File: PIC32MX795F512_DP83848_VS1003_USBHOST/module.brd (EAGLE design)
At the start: 109.9 x 68.6 mm, 116 parts, among them IC1 IC_USBLC6-2, IC2 LM1117IMPX-3.3, IC3 PIC32MX795F512, IC4 DP83848, IC5 LM1117MPX-2.5, U1 USD-SOCKETUSD, U2 VS1003, X2 CRYSTALS-NOGND-CFPX-217, X3 KUSBVX, Y1 CRYSTAL-GROUNDEDSMD-5X3.2, Y3 CRYSTAL-GROUNDEDSMD-5X3.2

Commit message: PCB updates
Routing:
- net GND: track 72.8 -> 73.7 mm
- added copper zone on layer 1, net N$4
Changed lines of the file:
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@@
 <wire x1="49.492" y1="48.3488" x2="48.88" y2="48.9608" width="0.2032" layer="1"/>
 <wire x1="47.468" y1="48.9608" x2="48.88" y2="48.9608" width="0.2032" layer="1"/>
-<wire x1="43.692" y1="42.0938" x2="45.5362" y2="42.0938" width="0.2032" layer="1"/>
-<wire x1="45.5362" y1="42.0938" x2="45.72" y2="41.91" width="0.2032" layer="1"/>
 <wire x1="55.092" y1="32.6938" x2="57.3304" y2="32.6938" width="0.19811875" layer="1"/>
 <via x="26.5324" y="34.7218" extent="1-16" drill="0.6" diameter="1.4224" shape="octagon"/>
@@
 <contactref element="SV1" pad="6"/>
 <contactref element="SV1" pad="4"/>
+<wire x1="43.692" y1="40.0938" x2="46.7614" y2="40.0938" width="0.2032" layer="1"/>
 </signal>
 <signal name="3V">
@@
 <wire x1="8.6868" y1="35.7632" x2="8.6868" y2="35.7736" width="0.3048" layer="1"/>
 </signal>
+<signal name="N$4">
+<polygon width="0" layer="1" pour="cutout">
+<vertex x="42.164" y="42.4434"/>
+<vertex x="42.164" y="39.37"/>
+<vertex x="45.2628" y="39.37"/>
+<vertex x="45.2628" y="42.4434"/>
+</polygon>
+</signal>
 </signals>

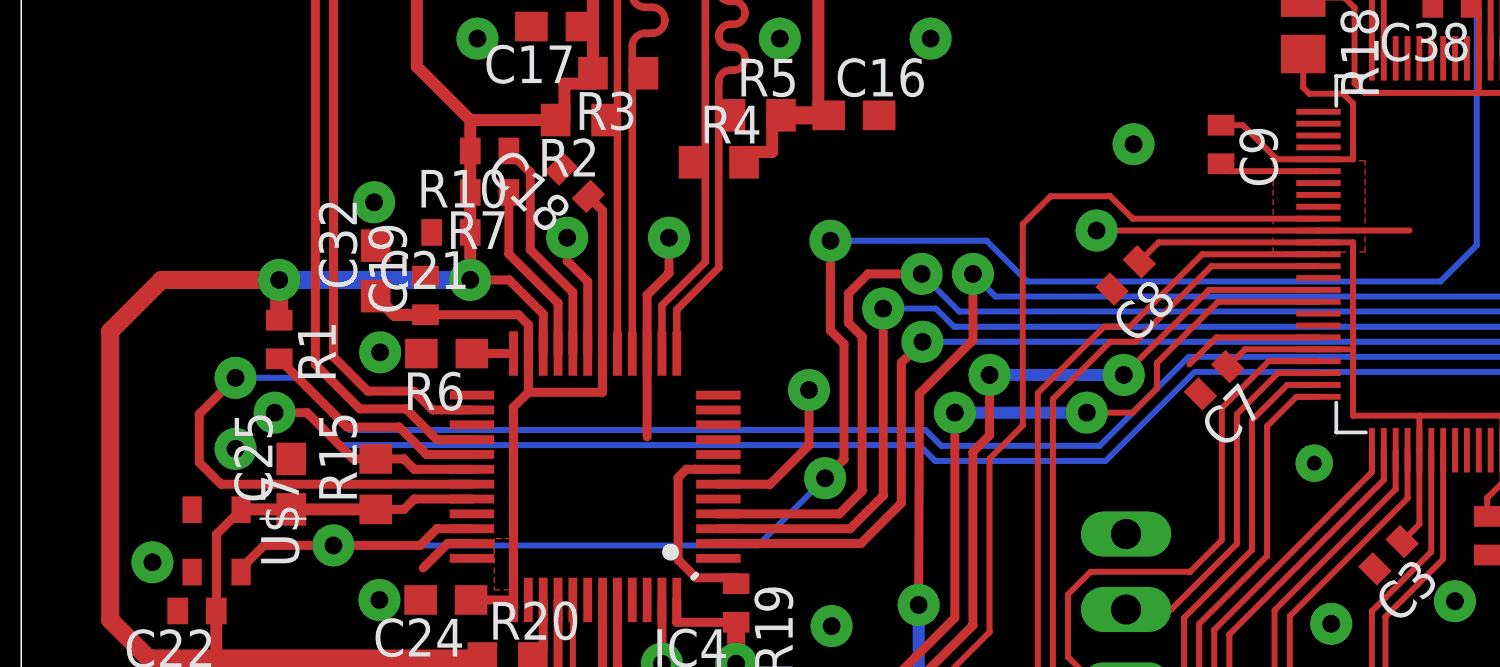
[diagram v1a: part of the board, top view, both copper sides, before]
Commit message: DP83848 RST line added
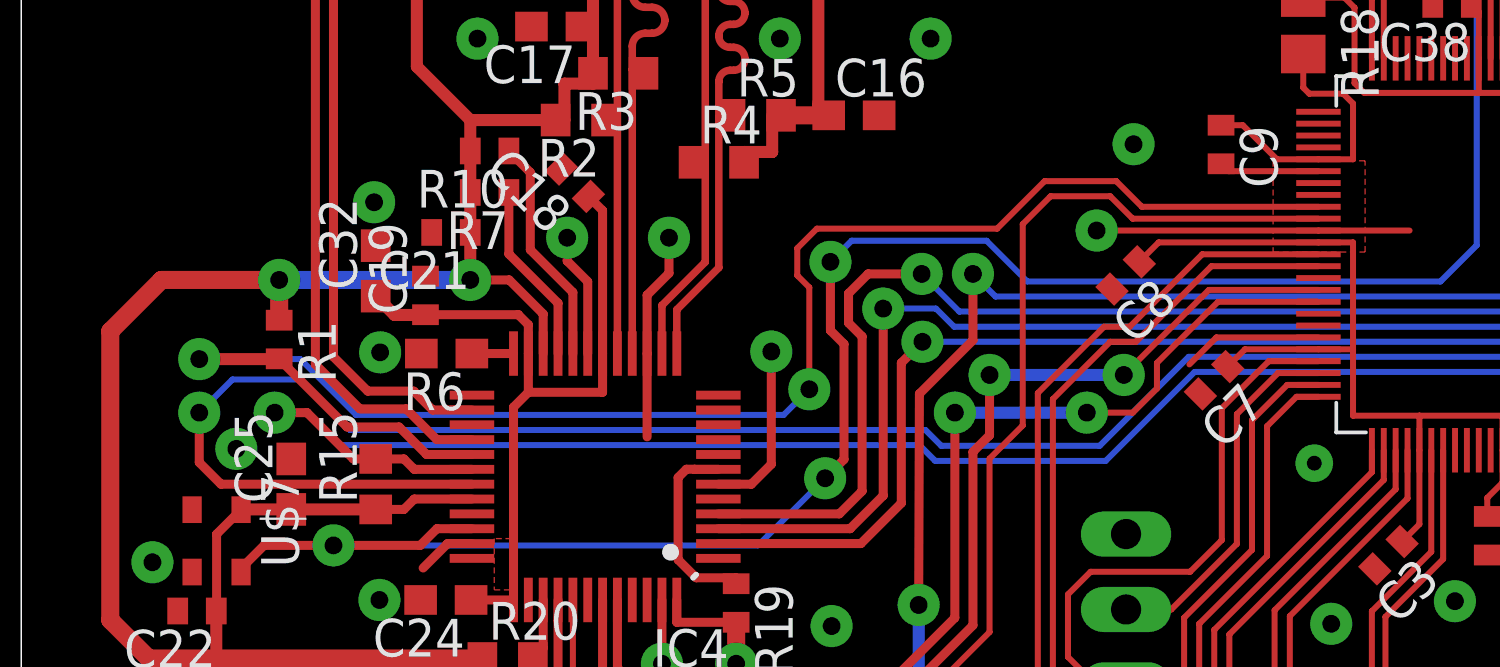
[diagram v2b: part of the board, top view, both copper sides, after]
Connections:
- removed net N$2: IC4.29, R1.2
- new net DP_RST: IC3.34, IC4.29, R1.2
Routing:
- net DP_RST: track 0.00 -> 56.0 mm, vias 0 -> 2
- net N$2: track 7.83 -> 0.00 mm
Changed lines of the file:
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@@
 <wire x1="18.387" y1="39.0678" x2="19.0794" y2="38.3754" width="0.3048" layer="1"/>
 <contactref element="U$7" pad="2"/>
-<via x="7.2176" y="32.7406" extent="1-16" drill="0.6" diameter="1.4224" shape="octagon"/>
+<via x="7.243" y="32.7406" extent="1-16" drill="0.6" diameter="1.4224" shape="octagon"/>
 <via x="4.417" y="28.9208" extent="1-16" drill="0.6" diameter="1.4224" shape="octagon"/>
 <via x="15.3644" y="46.5582" extent="1-16" drill="0.6" diameter="1.4224" shape="octagon"/>
@@
 <wire x1="47.468" y1="48.9608" x2="48.88" y2="48.9608" width="0.2032" layer="1"/>
 <wire x1="55.092" y1="32.6938" x2="57.3304" y2="32.6938" width="0.19811875" layer="1"/>
-<via x="26.5324" y="34.7218" extent="1-16" drill="0.6" diameter="1.4224" shape="octagon"/>
+<via x="25.2624" y="36.0172" extent="1-16" drill="0.6" diameter="1.4224" shape="octagon"/>
 <wire x1="21.0794" y1="35.9508" x2="21.0794" y2="33.1444" width="0.3048" layer="1"/>
 <via x="27.2944" y="26.7716" extent="1-16" drill="0.6" diameter="1.4224" shape="octagon"/>
@@
 <wire x1="43.692" y1="40.0938" x2="36.2204" y2="40.0938" width="0.2032" layer="1"/>
 <via x="54.384" y="19.431" extent="1-16" drill="0.6" diameter="1.4224" shape="octagon"/>
-<wire x1="23.4794" y1="31.5508" x2="25.2262" y2="31.5508" width="0.3048" layer="1"/>
-<wire x1="25.2262" y1="31.5508" x2="26.5324" y2="32.857" width="0.3048" layer="1"/>
-<wire x1="26.5324" y1="34.7218" x2="26.5324" y2="32.857" width="0.3048" layer="1"/>
+<wire x1="23.4794" y1="31.5508" x2="24.5912" y2="31.5508" width="0.3048" layer="1"/>
+<wire x1="24.5912" y1="31.5508" x2="25.2624" y2="32.222" width="0.3048" layer="1"/>
 <via x="59.5656" y="24.7396" extent="1-16" drill="0.6" diameter="1.4224" shape="octagon"/>
 <contactref element="SV1" pad="5"/>
@@
 <contactref element="SV1" pad="4"/>
 <wire x1="43.692" y1="40.0938" x2="46.7614" y2="40.0938" width="0.2032" layer="1"/>
+<wire x1="25.2624" y1="36.0172" x2="25.2624" y2="32.222" width="0.3048" layer="1"/>
 </signal>
 <signal name="3V">
@@
 <wire x1="27.7114" y1="32.385" x2="27.7114" y2="36.2712" width="0.3048" layer="1"/>
 <wire x1="27.7114" y1="36.2712" x2="27.2542" y2="36.7284" width="0.3048" layer="1"/>
-<via x="27.2542" y="39.751" extent="1-16" drill="0.6" diameter="1.4224" shape="octagon"/>
-<wire x1="27.2542" y1="36.7284" x2="27.2542" y2="39.751" width="0.3048" layer="1"/>
-<wire x1="32.512" y1="39.751" x2="27.2542" y2="39.751" width="0.2032" layer="16"/>
+<via x="27.2542" y="39.0398" extent="1-16" drill="0.6" diameter="1.4224" shape="octagon"/>
 <wire x1="15.1794" y1="30.0508" x2="13.9994" y2="30.0508" width="0.3048" layer="1"/>
 <wire x1="13.9994" y1="30.0508" x2="13.438" y2="29.4894" width="0.3048" layer="1"/>
+<wire x1="27.2542" y1="36.7284" x2="27.2542" y2="39.0398" width="0.3048" layer="1"/>
+<wire x1="32.512" y1="39.751" x2="27.9654" y2="39.751" width="0.2032" layer="16"/>
+<wire x1="27.9654" y1="39.751" x2="27.2542" y2="39.0398" width="0.2032" layer="16"/>
 </signal>
 <signal name="LED_ACT">
@@
 <wire x1="56.0578" y1="24.7396" x2="54.7878" y2="24.7396" width="0.2032" layer="1"/>
 <wire x1="54.7878" y1="24.7396" x2="53.492" y2="26.0354" width="0.2032" layer="1"/>
-<via x="7.2176" y="35.1322" extent="1-16" drill="0.6" diameter="1.4224" shape="octagon"/>
+<via x="5.9944" y="33.9598" extent="1-16" drill="0.6" diameter="1.4224" shape="octagon"/>
 <wire x1="15.1794" y1="31.5508" x2="6.727" y2="31.5508" width="0.3048" layer="1"/>
 <wire x1="6.727" y1="31.5508" x2="5.9944" y2="32.2834" width="0.3048" layer="1"/>
-<wire x1="9.3178" y1="35.1322" x2="11.0744" y2="33.3756" width="0.2032" layer="16"/>
-<wire x1="9.3178" y1="35.1322" x2="7.2176" y2="35.1322" width="0.2032" layer="16"/>
+<wire x1="9.3726" y1="35.0774" x2="11.0744" y2="33.3756" width="0.2032" layer="16"/>
 <wire x1="11.0744" y1="33.3756" x2="30.4546" y2="33.3756" width="0.2032" layer="16"/>
 <wire x1="30.4546" y1="33.3756" x2="30.988" y2="32.8422" width="0.2032" layer="16"/>
@@
 <wire x1="36.322" y1="32.8422" x2="39.3192" y2="35.8394" width="0.2032" layer="16"/>
 <wire x1="39.3192" y1="35.8394" x2="51.435" y2="35.8394" width="0.2032" layer="16"/>
-<wire x1="5.9944" y1="32.2834" x2="5.9944" y2="33.909" width="0.3048" layer="1"/>
-<wire x1="5.9944" y1="33.909" x2="7.2176" y2="35.1322" width="0.3048" layer="1"/>
+<wire x1="5.9944" y1="32.2834" x2="5.9944" y2="33.9598" width="0.3048" layer="1"/>
 <wire x1="56.0578" y1="24.7396" x2="53.3654" y2="24.7396" width="0.2032" layer="16"/>
 <wire x1="53.3654" y1="24.7396" x2="52.8066" y2="25.2984" width="0.2032" layer="16"/>
 <wire x1="52.8066" y1="25.2984" x2="52.8066" y2="34.4678" width="0.2032" layer="16"/>
 <wire x1="51.435" y1="35.8394" x2="52.8066" y2="34.4678" width="0.2032" layer="16"/>
+<wire x1="9.3726" y1="35.0774" x2="7.112" y2="35.0774" width="0.2032" layer="16"/>
+<wire x1="7.112" y1="35.0774" x2="5.9944" y2="33.9598" width="0.2032" layer="16"/>
 </signal>
 <signal name="RX_DV">
@@
 <wire x1="42.2148" y1="27.305" x2="46.292" y2="31.3822" width="0.2032" layer="1"/>
 </signal>
-<signal name="N$2">
+<signal name="DP_RST">
 <contactref element="R1" pad="2"/>
 <contactref element="IC4" pad="29"/>
@@
 <wire x1="10.9728" y1="33.4772" x2="8.6868" y2="35.7632" width="0.3048" layer="1"/>
 <wire x1="8.6868" y1="35.7632" x2="8.6868" y2="35.7736" width="0.3048" layer="1"/>
+<via x="5.9944" y="35.7632" extent="1-16" drill="0.6" diameter="1.4224" shape="octagon"/>
+<wire x1="5.9944" y1="35.7632" x2="8.6764" y2="35.7632" width="0.4064" layer="1"/>
+<wire x1="8.6764" y1="35.7632" x2="8.6868" y2="35.7736" width="0.4064" layer="1"/>
+<contactref element="IC3" pad="34"/>
+<via x="26.543" y="34.7472" extent="1-16" drill="0.6" diameter="1.4224" shape="octagon"/>
+<wire x1="26.543" y1="34.7472" x2="26.543" y2="38.1762" width="0.2032" layer="1"/>
+<wire x1="26.543" y1="38.1762" x2="26.1366" y2="38.5826" width="0.2032" layer="1"/>
+<wire x1="26.1366" y1="38.5826" x2="26.1366" y2="39.497" width="0.2032" layer="1"/>
+<wire x1="26.1366" y1="39.497" x2="26.797" y2="40.1574" width="0.2032" layer="1"/>
+<wire x1="26.797" y1="40.1574" x2="32.8676" y2="40.1574" width="0.2032" layer="1"/>
+<wire x1="43.692" y1="40.8938" x2="37.7446" y2="40.8938" width="0.2032" layer="1"/>
+<wire x1="37.7446" y1="40.8938" x2="36.8808" y2="41.7576" width="0.2032" layer="1"/>
+<wire x1="36.8808" y1="41.7576" x2="34.4678" y2="41.7576" width="0.2032" layer="1"/>
+<wire x1="32.8676" y1="40.1574" x2="34.4678" y2="41.7576" width="0.2032" layer="1"/>
+<wire x1="5.9944" y1="35.7632" x2="9.398" y2="35.7632" width="0.2032" layer="16"/>
+<wire x1="9.398" y1="35.7632" x2="11.2776" y2="33.8836" width="0.2032" layer="16"/>
+<wire x1="11.2776" y1="33.8836" x2="25.6794" y2="33.8836" width="0.2032" layer="16"/>
+<wire x1="25.6794" y1="33.8836" x2="26.543" y2="34.7472" width="0.2032" layer="16"/>
 </signal>
 <signal name="N$4">

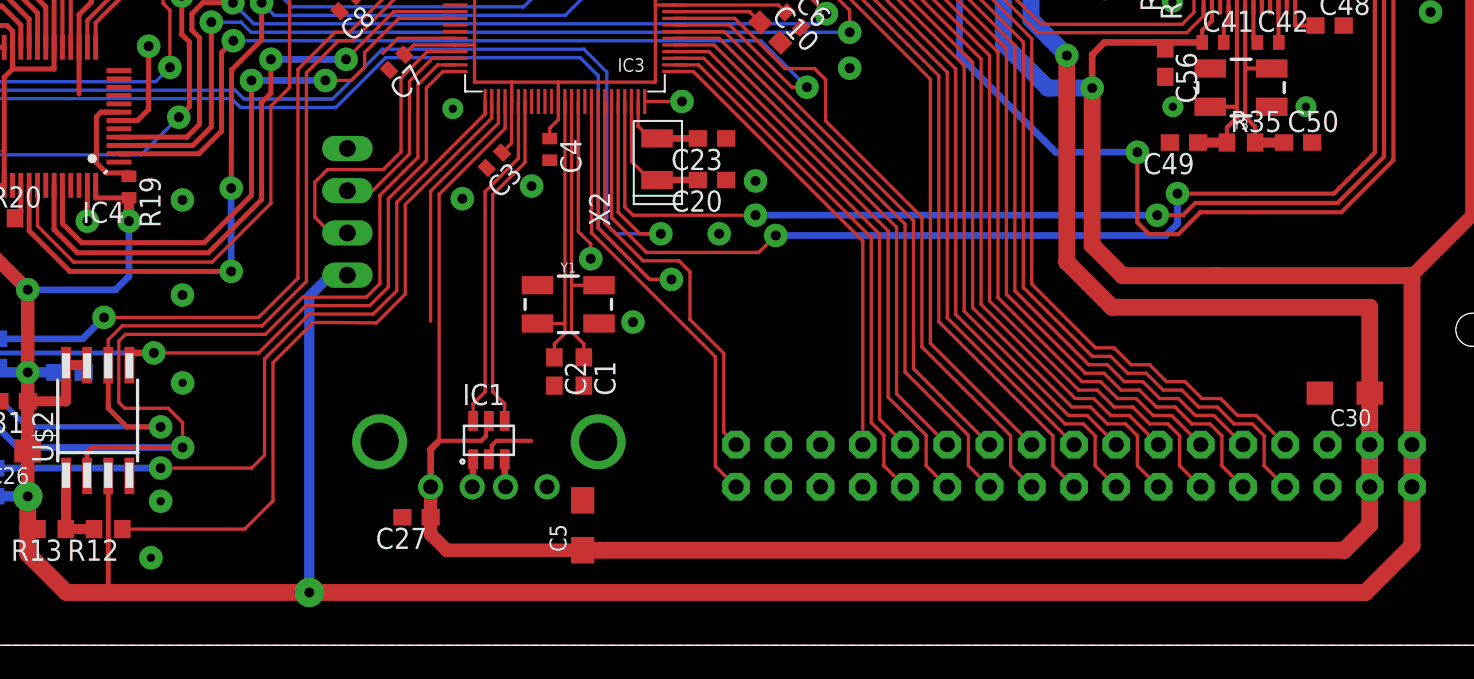
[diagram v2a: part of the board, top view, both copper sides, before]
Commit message: Crystl generator added
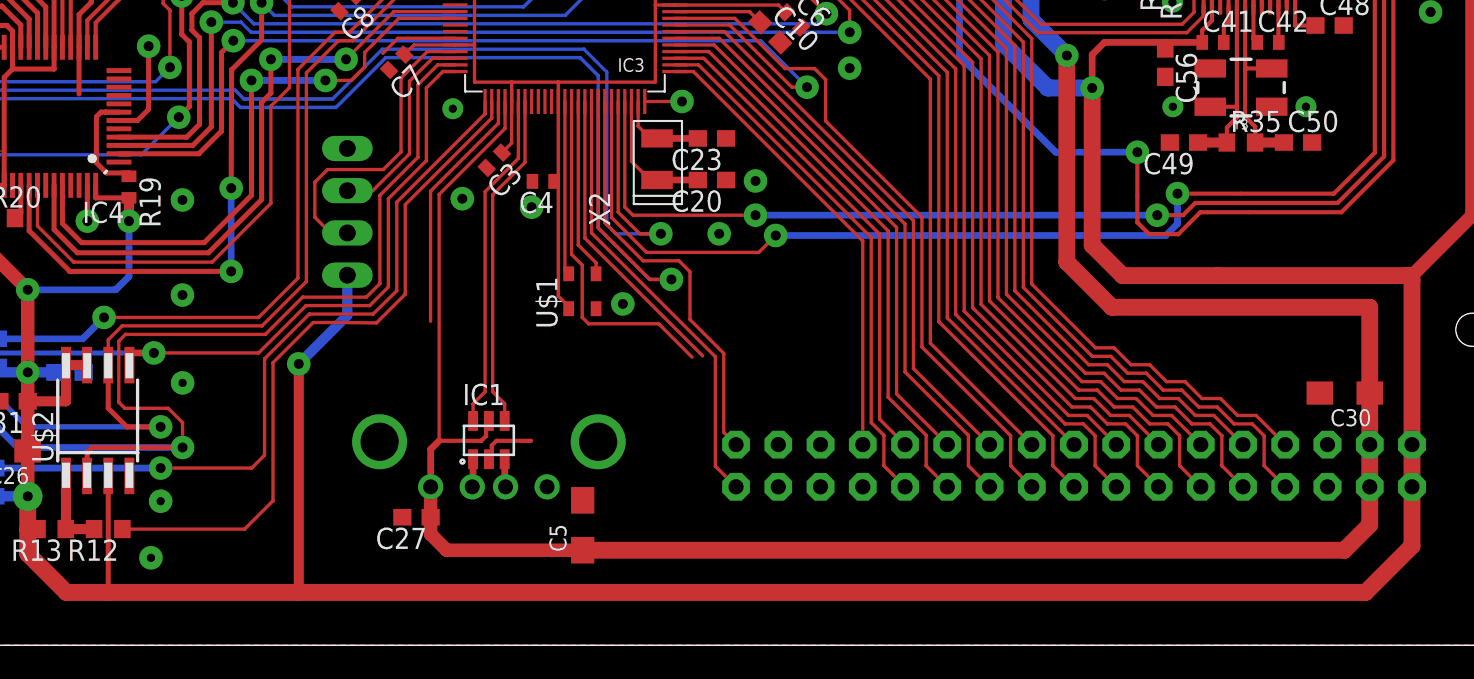
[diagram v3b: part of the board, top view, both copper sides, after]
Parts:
- removed C1, C2: 22 pF, rcl:C0603
- removed Y1: CRYSTAL-GROUNDEDSMD-5X3.2, SparkFun-Clocks:CRYSTAL-SMD-5X3.2-4PAD
- added U$1: ASE, crystal:ASE
- moved C4 1.96 mm to (49.0, 27.9), turned to 180 degrees
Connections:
- removed net OSC1: C2.1, IC3.63, Y1.1
- removed net OSC2: C1.1, IC3.64, Y1.3
- new net PH0: IC3.63, U$1.3
- new net RC15: IC3.64
- net 3V: now also U$1.4
- net GND: now also U$1.2; no longer C1.2, C2.2, Y1.2, Y1.4
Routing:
- net RC15: track 0.00 -> 20.8 mm
- net 1WIRE: track 0.00 -> 18.2 mm
- net OSC2: track 17.3 -> 0.00 mm
- net OSC1: track 17.3 -> 0.00 mm
- net PH0: track 0.00 -> 10.5 mm
- net 3V: track 549.2 -> 559.5 mm
- net GND: track 74.1 -> 75.2 mm, vias 43 -> 42

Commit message: Minor changes
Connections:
- removed net FLASH_CS_NOT: IC3.53
- new net SCL1A: IC3.53, SV1.1
- net 1WIRE: now also SV1.3
- net GND: no longer SV1.3, SV1.4, SV1.5, SV1.6, SV1.8
- net LED: now also SV1.6; no longer SV1.2
- net RC15: now also SV1.4
- net RD9: now also SV1.5; no longer SV1.1
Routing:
- net SCL1A: track 0.00 -> 14.9 mm
- net FLASH_CS_NOT: track 14.9 -> 0.00 mm
- net RC15: track 20.8 -> 33.5 mm
- net 1WIRE: track 18.2 -> 28.2 mm
- net LED: track 26.8 -> 31.6 mm
- net RD9: track 25.2 -> 28.9 mm
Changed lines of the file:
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@@
 <wire x1="24.5912" y1="31.5508" x2="25.2624" y2="32.222" width="0.3048" layer="1"/>
 <via x="59.5656" y="24.7396" extent="1-16" drill="0.6" diameter="1.4224" shape="octagon"/>
-<contactref element="SV1" pad="5"/>
-<contactref element="SV1" pad="3"/>
-<contactref element="SV1" pad="8"/>
-<contactref element="SV1" pad="6"/>
-<contactref element="SV1" pad="4"/>
 <wire x1="43.692" y1="40.0938" x2="46.7614" y2="40.0938" width="0.2032" layer="1"/>
 <wire x1="25.2624" y1="36.0172" x2="25.2624" y2="32.222" width="0.3048" layer="1"/>
@@
 <wire x1="52.692" y1="32.6938" x2="52.692" y2="25.413" width="0.2032" layer="1"/>
 <wire x1="52.692" y1="25.413" x2="54.991" y2="23.114" width="0.2032" layer="1"/>
-<contactref element="SV1" pad="1"/>
 <wire x1="54.991" y1="23.114" x2="57.15" y2="23.114" width="0.2032" layer="1"/>
 <wire x1="57.15" y1="23.114" x2="57.8104" y2="22.4536" width="0.2032" layer="1"/>
-<wire x1="57.8104" y1="22.4536" x2="57.8104" y2="19.5834" width="0.2032" layer="1"/>
-<wire x1="57.8104" y1="19.5834" x2="59.8424" y2="17.5514" width="0.2032" layer="1"/>
-<wire x1="59.8424" y1="17.5514" x2="59.8424" y2="12.8016" width="0.2032" layer="1"/>
-<wire x1="59.8424" y1="12.8016" x2="60.579" y2="12.065" width="0.2032" layer="1"/>
+<wire x1="57.8104" y1="22.4536" x2="57.8104" y2="21.4376" width="0.2032" layer="1"/>
+<contactref element="SV1" pad="5"/>
+<wire x1="57.8104" y1="21.4376" x2="58.3946" y2="20.8534" width="0.2032" layer="1"/>
+<wire x1="58.3946" y1="20.8534" x2="61.2394" y2="20.8534" width="0.2032" layer="1"/>
+<wire x1="61.2394" y1="20.8534" x2="63.373" y2="18.7198" width="0.2032" layer="1"/>
+<wire x1="63.373" y1="18.7198" x2="63.373" y2="14.351" width="0.2032" layer="1"/>
+<wire x1="63.373" y1="14.351" x2="65.659" y2="12.065" width="0.2032" layer="1"/>
 </signal>
 <signal name="LED">
 <contactref element="IC3" pad="67"/>
 <wire x1="51.892" y1="32.6938" x2="51.892" y2="24.7906" width="0.2032" layer="1"/>
-<wire x1="51.892" y1="24.7906" x2="59.3344" y2="17.3482" width="0.2032" layer="1"/>
-<contactref element="SV1" pad="2"/>
-<wire x1="60.579" y1="9.525" x2="59.3344" y2="10.7696" width="0.2032" layer="1"/>
-<wire x1="59.3344" y1="10.7696" x2="59.3344" y2="17.3482" width="0.2032" layer="1"/>
+<wire x1="51.892" y1="24.7906" x2="56.3372" y2="20.3454" width="0.2032" layer="1"/>
+<contactref element="SV1" pad="6"/>
+<wire x1="56.3372" y1="20.3454" x2="61.0362" y2="20.3454" width="0.2032" layer="1"/>
+<wire x1="61.0362" y1="20.3454" x2="62.865" y2="18.5166" width="0.2032" layer="1"/>
+<wire x1="62.865" y1="18.5166" x2="62.865" y2="14.1224" width="0.2032" layer="1"/>
+<wire x1="62.865" y1="14.1224" x2="64.389" y2="12.5984" width="0.2032" layer="1"/>
+<wire x1="64.389" y1="12.5984" x2="64.389" y2="10.795" width="0.2032" layer="1"/>
+<wire x1="64.389" y1="10.795" x2="65.659" y2="9.525" width="0.2032" layer="1"/>
 </signal>
 <signal name="1WIRE">
 <contactref element="IC3" pad="66"/>
 <wire x1="51.492" y1="32.6938" x2="51.492" y2="24.4794" width="0.2032" layer="1"/>
-<wire x1="51.492" y1="24.4794" x2="58.5724" y2="17.399" width="0.2032" layer="1"/>
+<contactref element="SV1" pad="3"/>
+<wire x1="51.492" y1="24.4794" x2="56.134" y2="19.8374" width="0.2032" layer="1"/>
+<wire x1="56.134" y1="19.8374" x2="60.833" y2="19.8374" width="0.2032" layer="1"/>
+<wire x1="60.833" y1="19.8374" x2="62.357" y2="18.3134" width="0.2032" layer="1"/>
+<wire x1="62.357" y1="18.3134" x2="62.357" y2="12.827" width="0.2032" layer="1"/>
+<wire x1="62.357" y1="12.827" x2="63.119" y2="12.065" width="0.2032" layer="1"/>
 </signal>
 <signal name="AN_3V">
@@
 <wire x1="28.702" y1="63.0682" x2="30.2768" y2="64.643" width="0.4064" layer="1"/>
 </signal>
-<signal name="FLASH_CS_NOT">
+<signal name="SCL1A">
 <contactref element="IC3" pad="53"/>
 <wire x1="46.292" y1="32.6938" x2="46.292" y2="31.3822" width="0.2032" layer="1"/>
 <wire x1="42.2148" y1="27.305" x2="46.292" y2="31.3822" width="0.2032" layer="1"/>
 <wire x1="42.2148" y1="27.305" x2="42.2148" y2="19.4818" width="0.2032" layer="1"/>
+<contactref element="SV1" pad="1"/>
+<wire x1="42.2148" y1="19.4818" x2="60.579" y2="12.065" width="0" layer="19" extent="1-1"/>
 </signal>
 <signal name="DP_RST">
@@
 <wire x1="51.3334" y1="22.86" x2="51.3334" y2="19.7104" width="0.2032" layer="1"/>
 <wire x1="51.3334" y1="19.7104" x2="51.7144" y2="19.3294" width="0.2032" layer="1"/>
-<wire x1="51.7144" y1="19.3294" x2="55.9308" y2="19.3294" width="0.2032" layer="1"/>
-<wire x1="55.9308" y1="19.3294" x2="57.9374" y2="17.3228" width="0.2032" layer="1"/>
+<contactref element="SV1" pad="4"/>
+<wire x1="51.7144" y1="19.3294" x2="60.6298" y2="19.3294" width="0.2032" layer="1"/>
+<wire x1="60.6298" y1="19.3294" x2="61.849" y2="18.1102" width="0.2032" layer="1"/>
+<wire x1="61.849" y1="18.1102" x2="61.849" y2="10.795" width="0.2032" layer="1"/>
+<wire x1="61.849" y1="10.795" x2="63.119" y2="9.525" width="0.2032" layer="1"/>
 </signal>
 </signals>
